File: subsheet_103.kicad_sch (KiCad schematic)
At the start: 35 parts, among them T11 BC 547 B

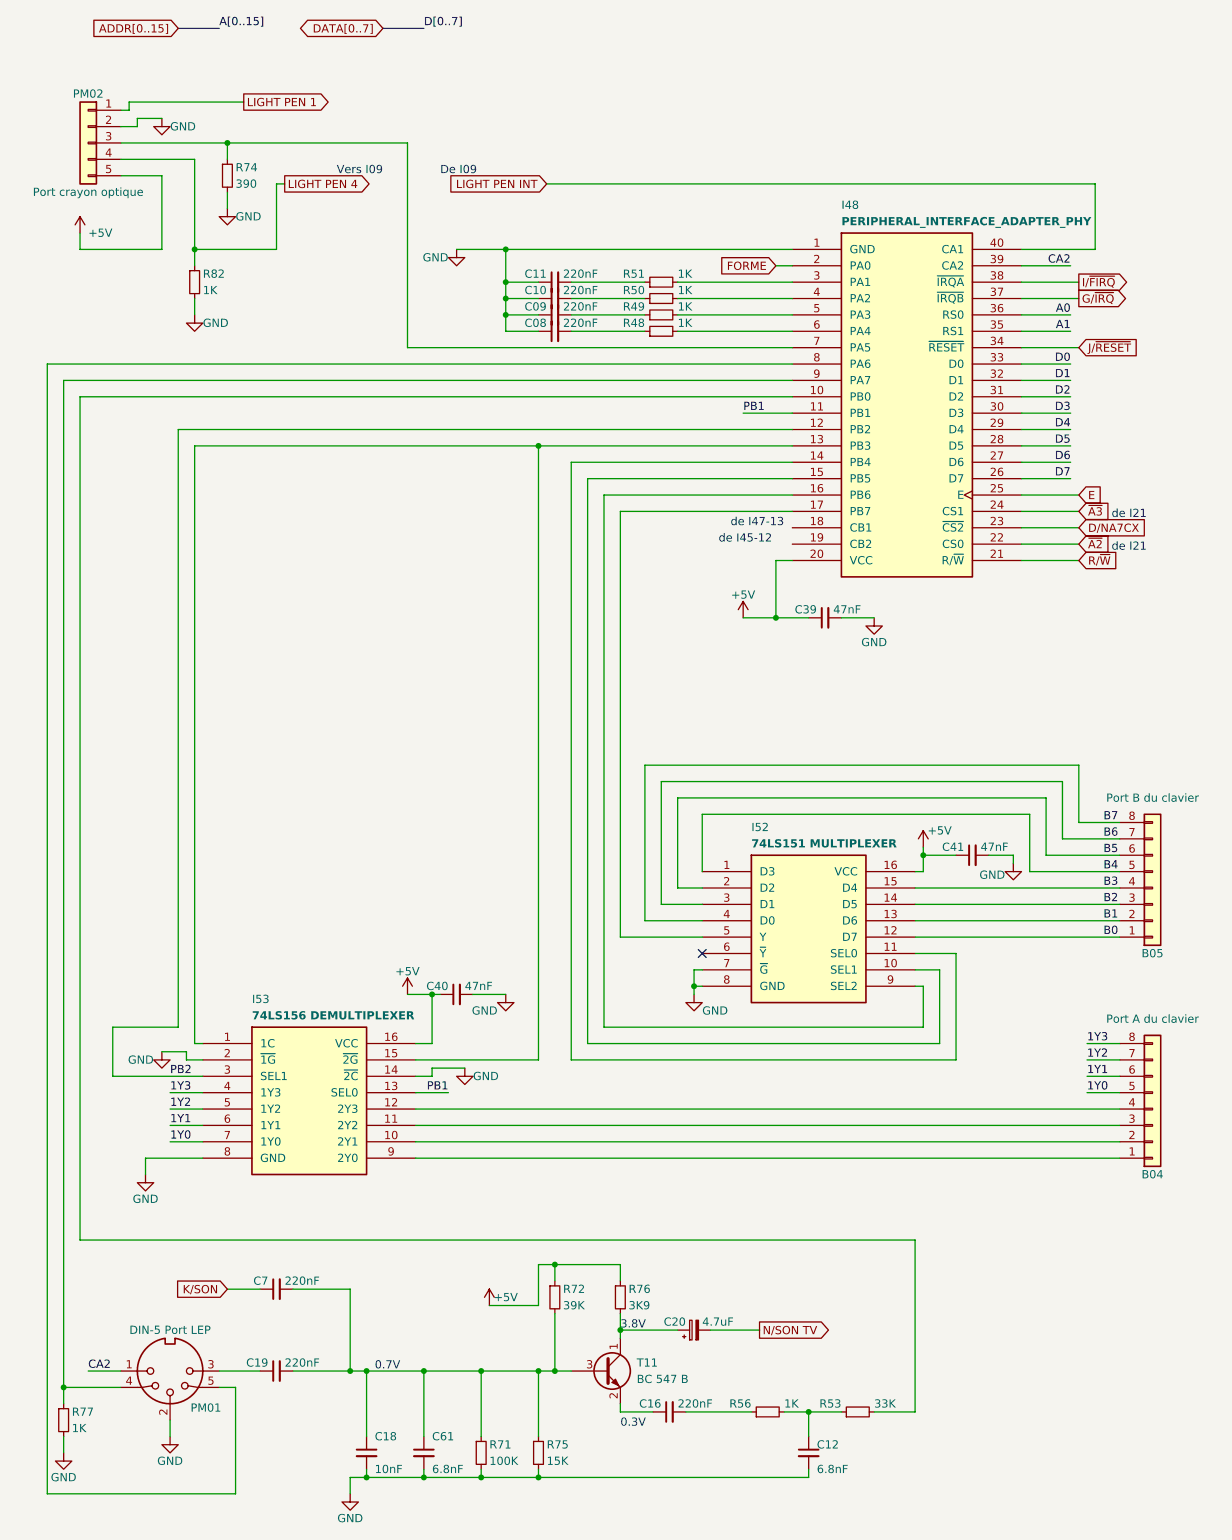
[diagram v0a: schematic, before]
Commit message: Nommage de signaux d'après documentations techniques
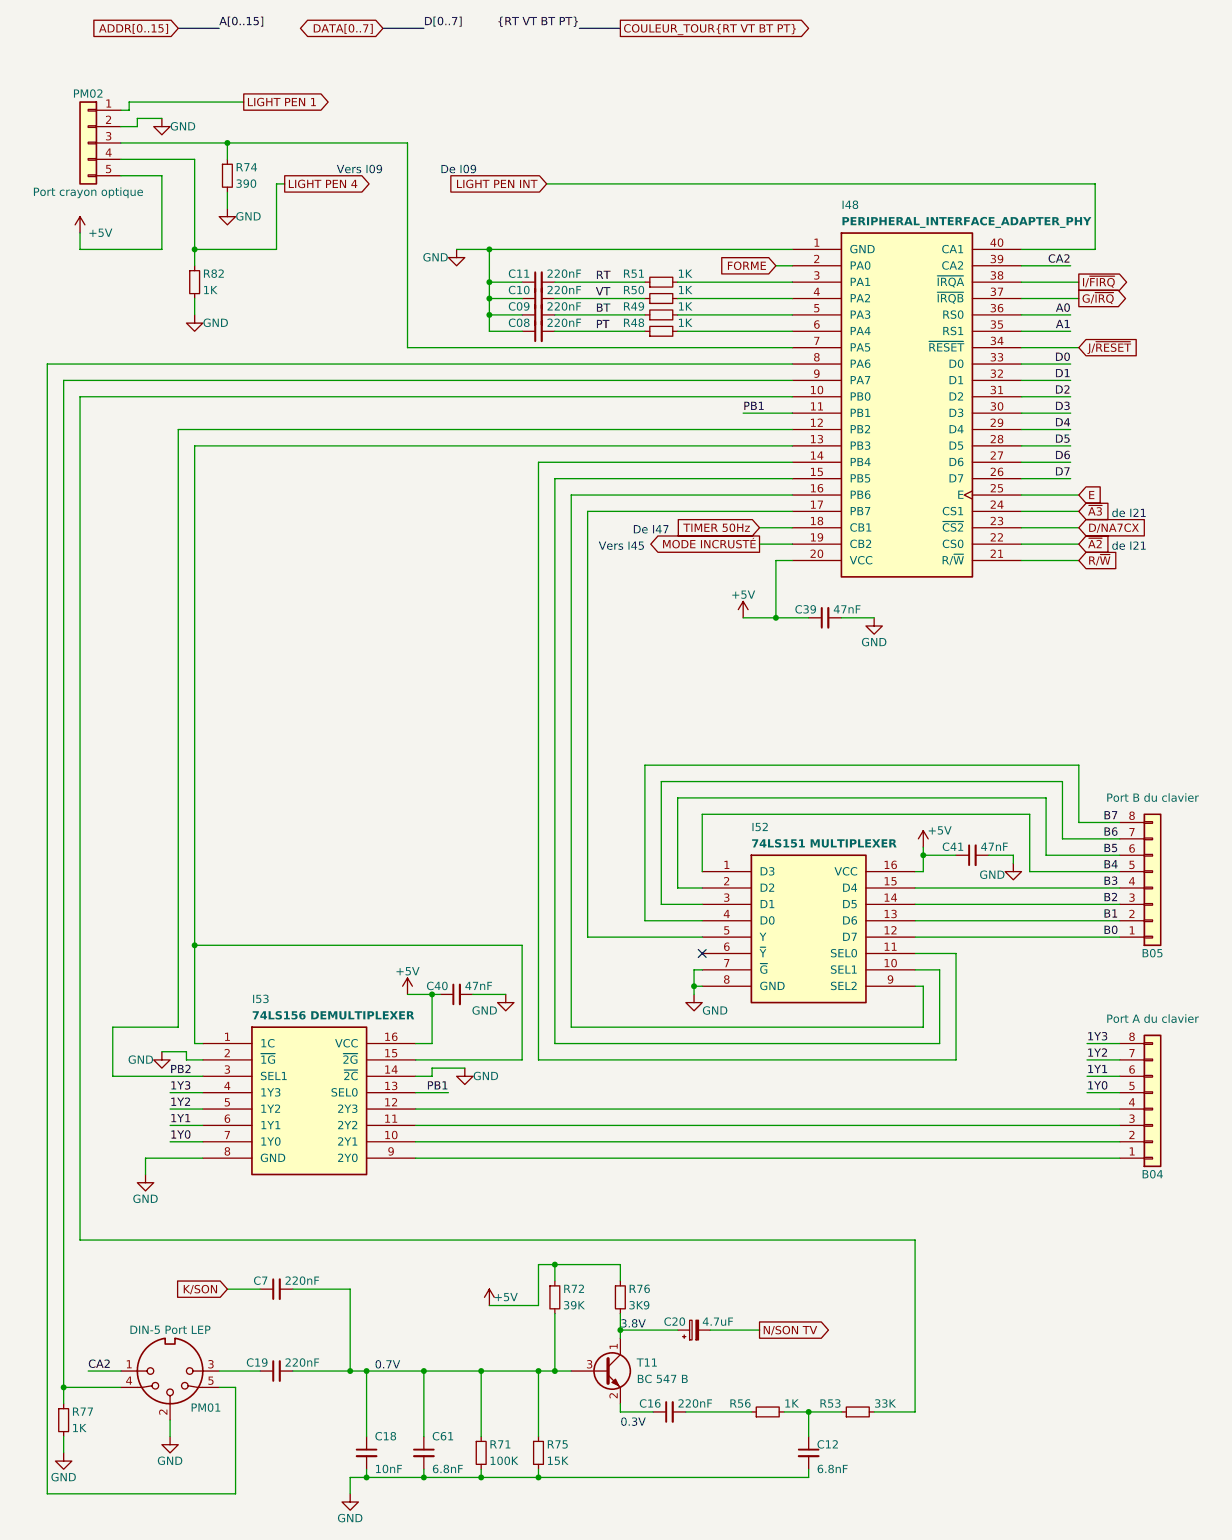
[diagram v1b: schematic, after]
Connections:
- net RT: now reaches C11.2, R51.1
- net BT: now reaches C09.2, R49.1
- net VT: now reaches C10.2, R50.1
- net TIMER 50Hz: now reaches I48.18 (CB1)
- net MODE INCRUSTÉ: now reaches I48.19 (CB2)
- net PT: now reaches C08.2, R48.1
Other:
- note added: "De I47"
- note added: "Vers I45"
- note removed: "de I45-12"
- note removed: "de I47-13"
- moved on the sheet: C08, C09, C10, C11

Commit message: retravaille les ports LEP et crayon optique pour correspondre visuellement (suppression de renversements)
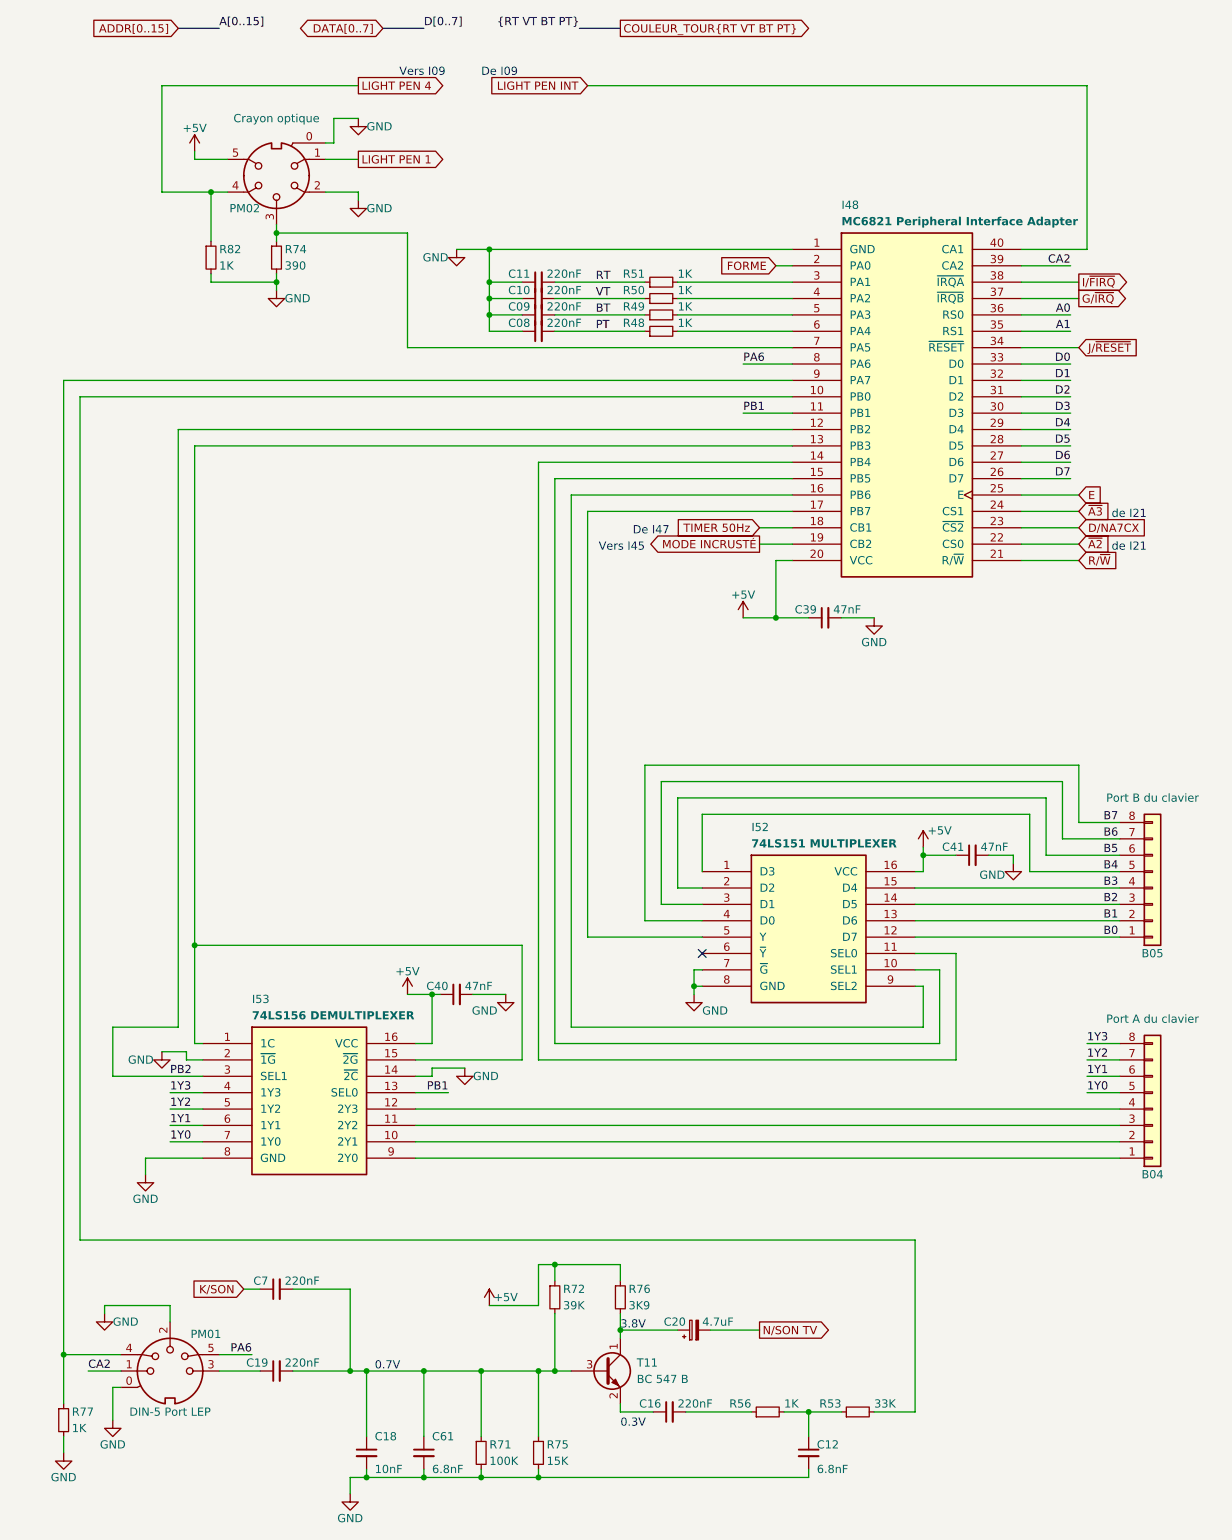
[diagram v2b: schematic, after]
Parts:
- removed PM02: Port crayon optique, symbol Connector_Generic:Conn_01x05
- added PM02: Crayon optique, symbol connectors_with_ground:DIN-5_GND
- I48: value PERIPHERAL_INTERFACE_ADAPTER_PHY -> MC6821 Peripheral Interface Adapter
- PM01: symbol Connector:DIN-5_180degree -> connectors_with_ground:DIN-5_180degree_GND
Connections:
- net +5V: now also PM02.5
- net GND: now also PM01.0, PM02.0, PM02.2
- net LIGHT PEN 1: now also PM02.1
- net LIGHT PEN 4: now also PM02.4
- net at I48.7 (PA5), R74.1: now also PM02.3
- net PA6: now reaches I48.8 (PA6), PM01.5
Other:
- moved on the sheet: R74, R82

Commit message: ports d'extension et cartouche
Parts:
- renumbered C7 to C17
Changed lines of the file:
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@@
   (symbol (lib_id "Device:C_Small") (at 53.34 220.98 90) (unit 1)
     (in_bom yes) (on_board yes)
-    (property "Reference" "C7" (id 0) (at 52.07 219.71 90)
+    (property "Reference" "C17" (id 0) (at 52.07 219.71 90)
       (effects (font (size 1.27 1.27)) (justify left))
     )

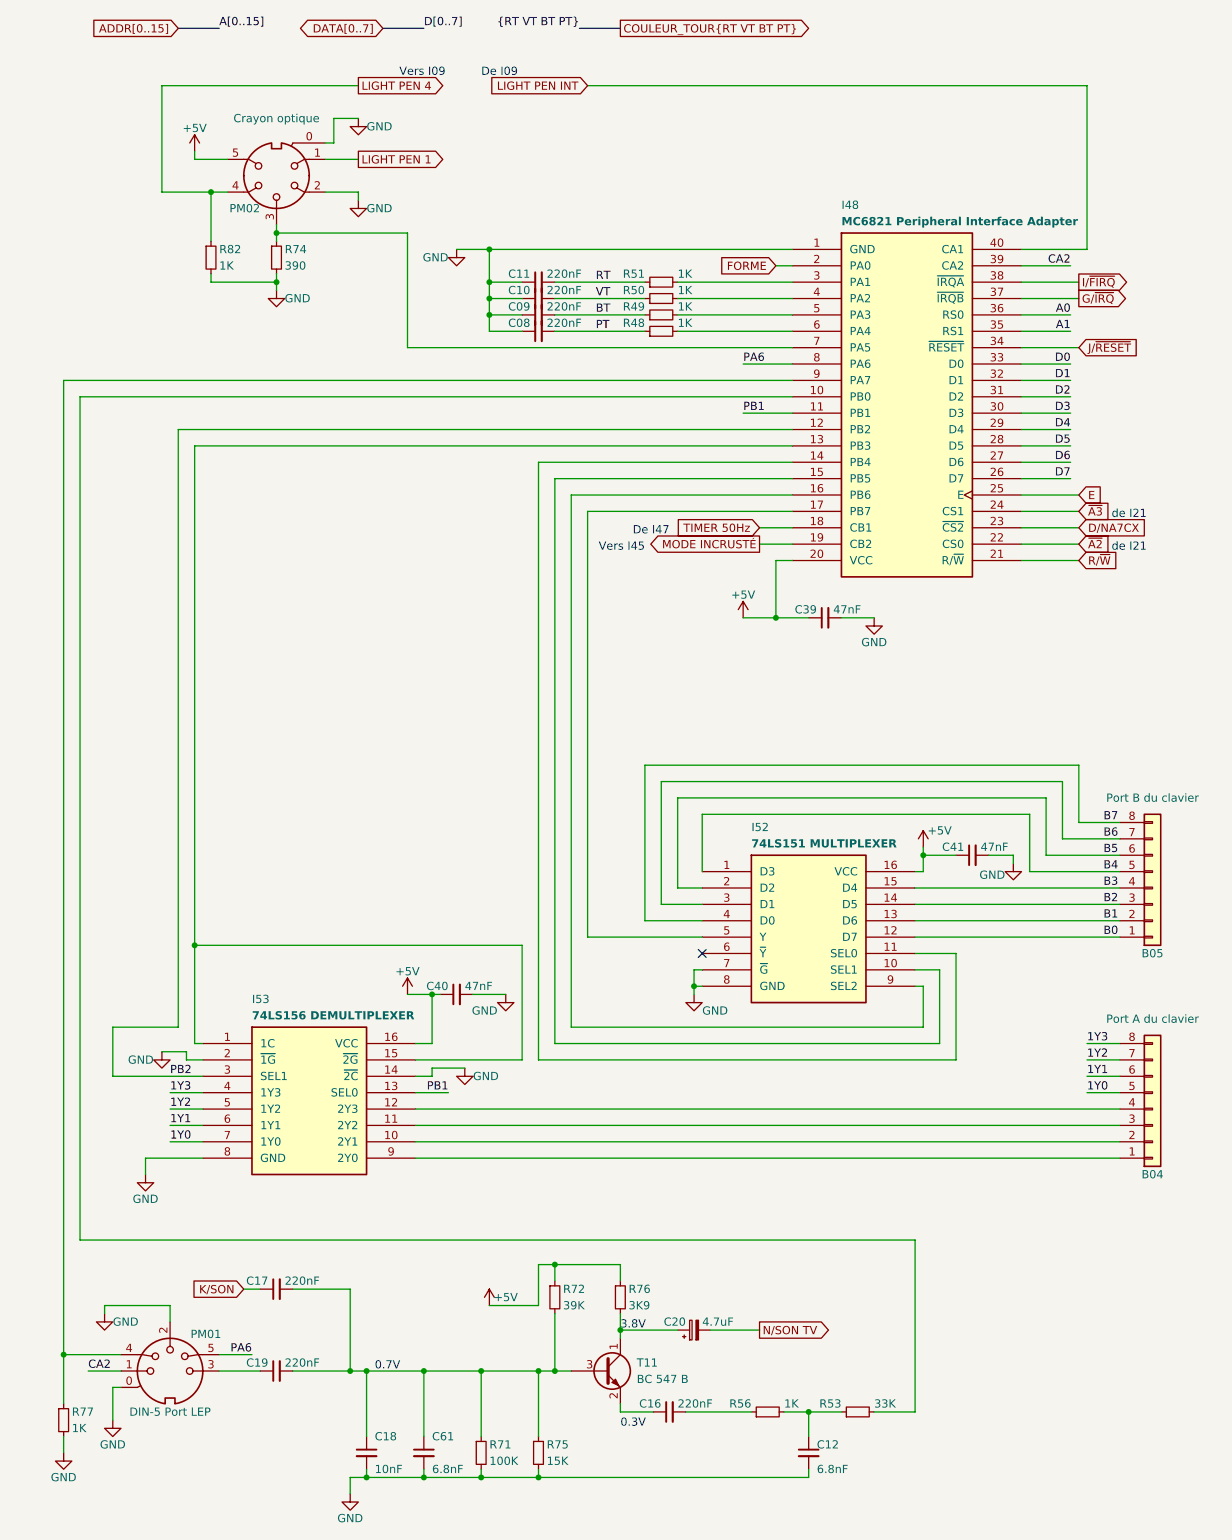
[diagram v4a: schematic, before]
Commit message: decodage d'addresse, re-pagination
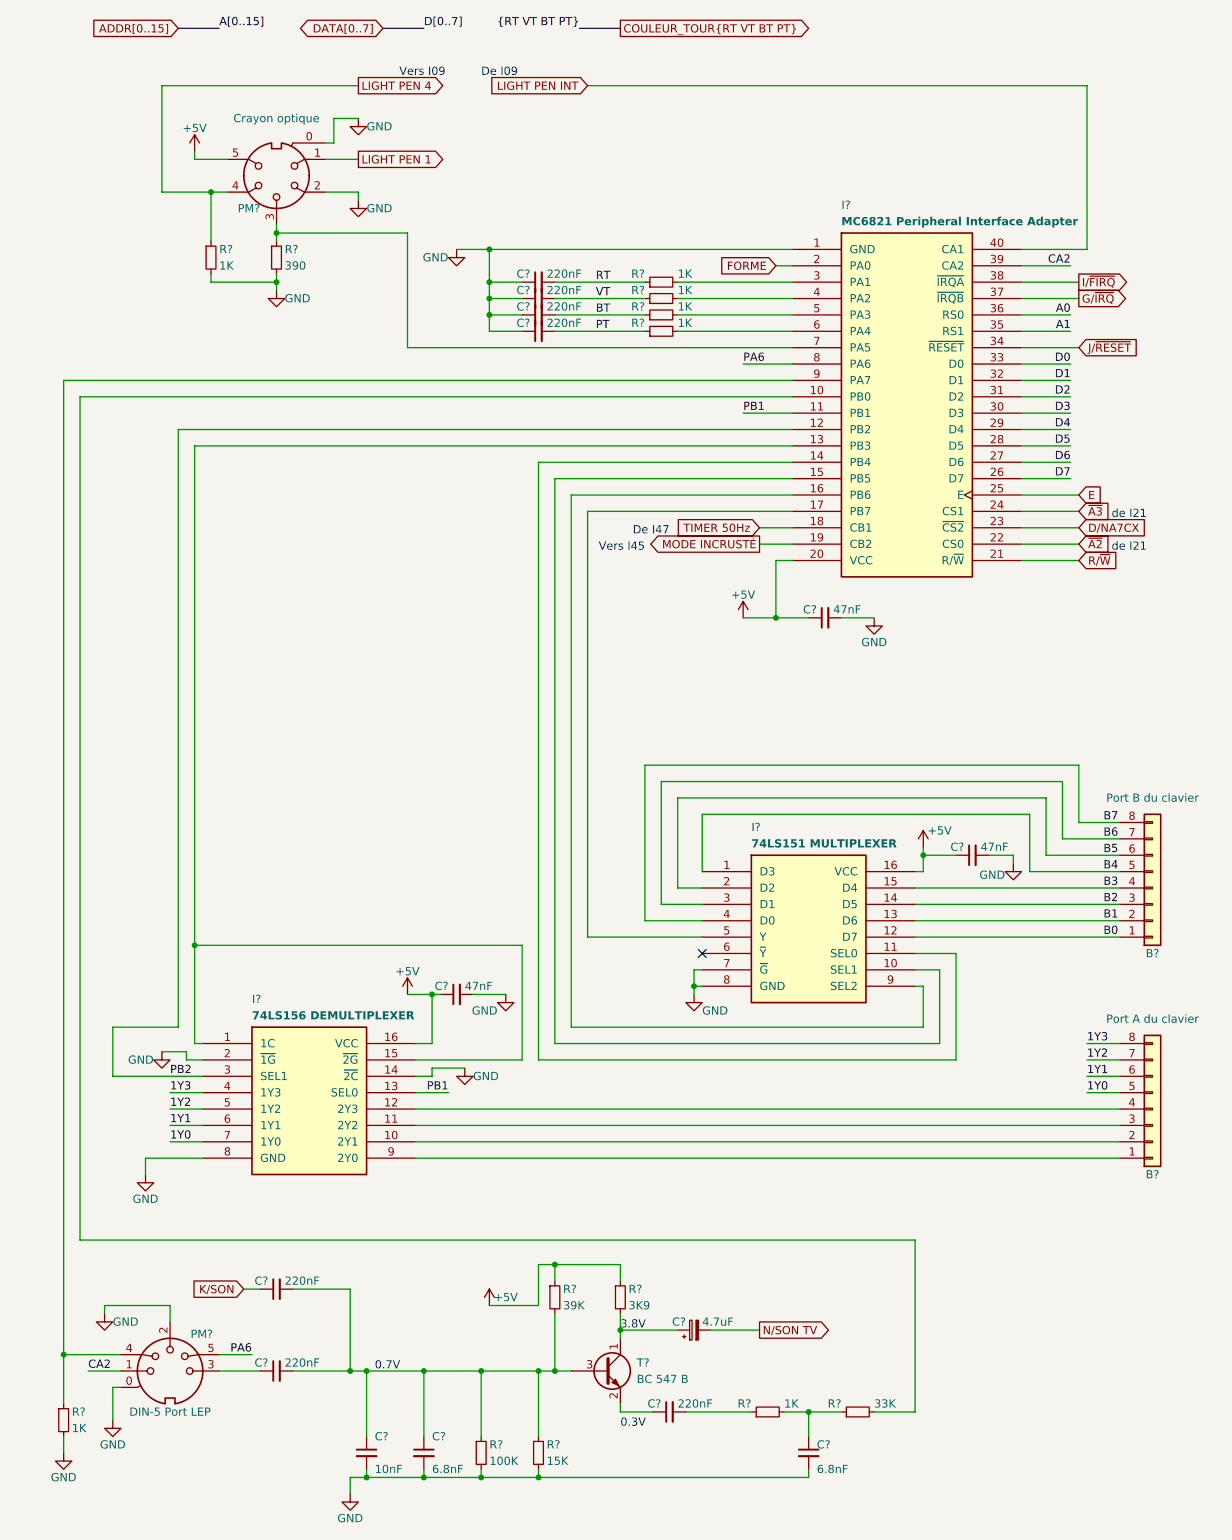
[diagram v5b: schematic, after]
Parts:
- renumbered B04 to B?, B05 to B?, C11 to C?, C61 to C?, C17 to C?, C40 to C?, C12 to C?, C41 to C?, C19 to C?, C09 to C?, C39 to C?, C10 to C?, C18 to C?, C20 to C?, C08 to C?, C16 to C?, I53 to I?, I52 to I?, I48 to I?, PM02 to PM?, PM01 to PM?, R56 to R?, R77 to R?, R71 to R?, R75 to R?, R72 to R?, R51 to R?, R76 to R?, R49 to R?, R50 to R?, R82 to R?, R53 to R?, R74 to R?, R48 to R?, T11 to T?

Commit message: prepare release
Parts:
- gave numbers to parts that had none: 35
